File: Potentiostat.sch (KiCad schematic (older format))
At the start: 16 parts, among them U4 MAX6071BAUT21T, U5 LMP91000, U6 SPEC-110-902, U7 MCP6041T-I_OT

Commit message: layout wip
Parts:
- renumbered C10 to C11, C11 to C12, C12 to C13, C13 to C14, C14 to C15, C15 to C16, C16 to C17, R11 to R13, R12 to R14, R13 to R15, R14 to R16, R15 to R17, U4 to U5, U5 to U6, U6 to U7, U7 to U8
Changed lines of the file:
@@
 P 5800 4050
 AR Path="/605CEBF3" Ref="U?"  Part="1"
-AR Path="/605B4CA4/605CEBF3" Ref="U5"  Part="1"
-F 0 "U5" H 5350 5000 50  0000 C CNN
+AR Path="/605B4CA4/605CEBF3" Ref="U6"  Part="1"
+F 0 "U6" H 5350 5000 50  0000 C CNN
 F 1 "LMP91000" H 5850 5000 50  0000 C CNN
 F 2 "JetkovKiCADLib:LMP91000" H 5300 2900 50  0001 L BNN
@@
 P 5050 4700
 AR Path="/605CEBFB" Ref="#PWR?"  Part="1"
-AR Path="/605B4CA4/605CEBFB" Ref="#PWR045"  Part="1"
-F 0 "#PWR045" H 5050 4450 50  0001 C CNN
+AR Path="/605B4CA4/605CEBFB" Ref="#PWR048"  Part="1"
+F 0 "#PWR048" H 5050 4450 50  0001 C CNN
 F 1 "GND" H 5055 4527 50  0000 C CNN
 F 2 "" H 5050 4700 50  0001 C CNN
@@
 P 6650 3550
 AR Path="/605CEC09" Ref="R?"  Part="1"
-AR Path="/605B4CA4/605CEC09" Ref="R14"  Part="1"
-F 0 "R14" H 6720 3596 50  0000 L CNN
+AR Path="/605B4CA4/605CEC09" Ref="R16"  Part="1"
+F 0 "R16" H 6720 3596 50  0000 L CNN
 F 1 "49R9" H 6720 3505 50  0000 L CNN
 F 2 "JetkovKiCADLib:R_0402_NoSilk" V 6580 3550 50  0001 C CNN
@@
 P 7450 3850
 AR Path="/605CEC15" Ref="U?"  Part="1"
-AR Path="/605B4CA4/605CEC15" Ref="U6"  Part="1"
-F 0 "U6" H 7200 4200 50  0000 C CNN
+AR Path="/605B4CA4/605CEC15" Ref="U7"  Part="1"
+F 0 "U7" H 7200 4200 50  0000 C CNN
 F 1 "SPEC-110-902" H 7450 3500 50  0000 C CNN
 F 2 "JetkovKiCADLib:SPEC-110-902" H 7200 3250 50  0001 L BNN
@@
 P 6550 4300
 AR Path="/605CEC24" Ref="R?"  Part="1"
-AR Path="/605B4CA4/605CEC24" Ref="R13"  Part="1"
-F 0 "R13" H 6620 4346 50  0000 L CNN
+AR Path="/605B4CA4/605CEC24" Ref="R15"  Part="1"
+F 0 "R15" H 6620 4346 50  0000 L CNN
 F 1 "499k" H 6620 4255 50  0000 L CNN
 F 2 "JetkovKiCADLib:R_0402_NoSilk" V 6480 4300 50  0001 C CNN
@@
 P 6750 4300
 AR Path="/605CEC2A" Ref="C?"  Part="1"
-AR Path="/605B4CA4/605CEC2A" Ref="C15"  Part="1"
-F 0 "C15" H 6865 4346 50  0000 L CNN
+AR Path="/605B4CA4/605CEC2A" Ref="C16"  Part="1"
+F 0 "C16" H 6865 4346 50  0000 L CNN
 F 1 "DNP" H 6865 4255 50  0000 L CNB
 F 2 "JetkovKiCADLib:C_0402_NoSilk" H 6788 4150 50  0001 C CNN
@@
 P 4600 3450
 AR Path="/605CEC3F" Ref="C?"  Part="1"
-AR Path="/605B4CA4/605CEC3F" Ref="C14"  Part="1"
-F 0 "C14" H 4715 3496 50  0000 L CNN
+AR Path="/605B4CA4/605CEC3F" Ref="C15"  Part="1"
+F 0 "C15" H 4715 3496 50  0000 L CNN
 F 1 "1u" H 4715 3405 50  0000 L CNN
 F 2 "JetkovKiCADLib:C_0402_NoSilk" H 4638 3300 50  0001 C CNN
@@
 P 4600 3600
 AR Path="/605CEC45" Ref="#PWR?"  Part="1"
-AR Path="/605B4CA4/605CEC45" Ref="#PWR044"  Part="1"
-F 0 "#PWR044" H 4600 3350 50  0001 C CNN
+AR Path="/605B4CA4/605CEC45" Ref="#PWR047"  Part="1"
+F 0 "#PWR047" H 4600 3350 50  0001 C CNN
 F 1 "GND" H 4605 3427 50  0000 C CNN
 F 2 "" H 4600 3600 50  0001 C CNN
@@
 P 2350 3950
 AR Path="/605CEC51" Ref="U?"  Part="1"
-AR Path="/605B4CA4/605CEC51" Ref="U4"  Part="1"
-F 0 "U4" H 1900 4500 50  0000 C CNN
+AR Path="/605B4CA4/605CEC51" Ref="U5"  Part="1"
+F 0 "U5" H 1900 4500 50  0000 C CNN
 F 1 "MAX6071BAUT21T" H 2118 3695 50  0000 C CNN
 F 2 "JetkovKiCADLib:MAX6071BAUT21" H 1850 3150 50  0001 L BNN
@@
 P 2600 4100
 AR Path="/605CEC5C" Ref="#PWR?"  Part="1"
-AR Path="/605B4CA4/605CEC5C" Ref="#PWR039"  Part="1"
-F 0 "#PWR039" H 2600 3850 50  0001 C CNN
+AR Path="/605B4CA4/605CEC5C" Ref="#PWR042"  Part="1"
+F 0 "#PWR042" H 2600 3850 50  0001 C CNN
 F 1 "GND" H 2605 3927 50  0000 C CNN
 F 2 "" H 2600 4100 50  0001 C CNN
@@
 P 2900 3750
 AR Path="/605CEC62" Ref="C?"  Part="1"
-AR Path="/605B4CA4/605CEC62" Ref="C11"  Part="1"
-F 0 "C11" H 3015 3796 50  0000 L CNN
+AR Path="/605B4CA4/605CEC62" Ref="C12"  Part="1"
+F 0 "C12" H 3015 3796 50  0000 L CNN
 F 1 "0.1u" H 3015 3705 50  0000 L CNN
 F 2 "JetkovKiCADLib:C_0402_NoSilk" H 2938 3600 50  0001 C CNN
@@
 P 1000 3750
 AR Path="/605CEC69" Ref="C?"  Part="1"
-AR Path="/605B4CA4/605CEC69" Ref="C10"  Part="1"
-F 0 "C10" H 1115 3796 50  0000 L CNN
+AR Path="/605B4CA4/605CEC69" Ref="C11"  Part="1"
+F 0 "C11" H 1115 3796 50  0000 L CNN
 F 1 "0.1u" H 1115 3705 50  0000 L CNN
 F 2 "JetkovKiCADLib:C_0402_NoSilk" H 1038 3600 50  0001 C CNN
@@
 P 1000 3900
 AR Path="/605CEC6F" Ref="#PWR?"  Part="1"
-AR Path="/605B4CA4/605CEC6F" Ref="#PWR037"  Part="1"
-F 0 "#PWR037" H 1000 3650 50  0001 C CNN
+AR Path="/605B4CA4/605CEC6F" Ref="#PWR040"  Part="1"
+F 0 "#PWR040" H 1000 3650 50  0001 C CNN
 F 1 "GND" H 1005 3727 50  0000 C CNN
 F 2 "" H 1000 3900 50  0001 C CNN
@@
 P 1650 4400
 AR Path="/605CEC76" Ref="#PWR?"  Part="1"
-AR Path="/605B4CA4/605CEC76" Ref="#PWR038"  Part="1"
-F 0 "#PWR038" H 1650 4150 50  0001 C CNN
+AR Path="/605B4CA4/605CEC76" Ref="#PWR041"  Part="1"
+F 0 "#PWR041" H 1650 4150 50  0001 C CNN
 F 1 "GND" H 1655 4227 50  0000 C CNN
 F 2 "" H 1650 4400 50  0001 C CNN
@@
 P 1650 4250
 AR Path="/605CEC7C" Ref="R?"  Part="1"
-AR Path="/605B4CA4/605CEC7C" Ref="R11"  Part="1"
-F 0 "R11" H 1720 4296 50  0000 L CNN
+AR Path="/605B4CA4/605CEC7C" Ref="R13"  Part="1"
+F 0 "R13" H 1720 4296 50  0000 L CNN
 F 1 "1M" H 1720 4205 50  0000 L CNN
 F 2 "JetkovKiCADLib:R_0402_NoSilk" V 1580 4250 50  0001 C CNN
@@
 P 1000 3500
 AR Path="/605CEC87" Ref="#PWR?"  Part="1"
-AR Path="/605B4CA4/605CEC87" Ref="#PWR036"  Part="1"
-F 0 "#PWR036" H 1000 3350 50  0001 C CNN
+AR Path="/605B4CA4/605CEC87" Ref="#PWR039"  Part="1"
+F 0 "#PWR039" H 1000 3350 50  0001 C CNN
 F 1 "VDD" H 1015 3673 50  0000 C CNN
 F 2 "" H 1000 3500 50  0001 C CNN
@@
 P 3200 3750
 AR Path="/605CEC91" Ref="R?"  Part="1"
-AR Path="/605B4CA4/605CEC91" Ref="R12"  Part="1"
-F 0 "R12" H 3270 3796 50  0000 L CNN
+AR Path="/605B4CA4/605CEC91" Ref="R14"  Part="1"
+F 0 "R14" H 3270 3796 50  0000 L CNN
 F 1 "DNP" H 3270 3705 50  0000 L CNB
 F 2 "JetkovKiCADLib:R_0402_NoSilk" V 3130 3750 50  0001 C CNN
@@
 P 3200 4050
 AR Path="/605CEC97" Ref="C?"  Part="1"
-AR Path="/605B4CA4/605CEC97" Ref="C12"  Part="1"
-F 0 "C12" H 3315 4096 50  0000 L CNN
+AR Path="/605B4CA4/605CEC97" Ref="C13"  Part="1"
+F 0 "C13" H 3315 4096 50  0000 L CNN
 F 1 "DNP" H 3315 4005 50  0000 L CNB
 F 2 "JetkovKiCADLib:C_0402_NoSilk" H 3238 3900 50  0001 C CNN
@@
 P 3200 4200
 AR Path="/605CEC9D" Ref="#PWR?"  Part="1"
-AR Path="/605B4CA4/605CEC9D" Ref="#PWR041"  Part="1"
-F 0 "#PWR041" H 3200 3950 50  0001 C CNN
+AR Path="/605B4CA4/605CEC9D" Ref="#PWR044"  Part="1"
+F 0 "#PWR044" H 3200 3950 50  0001 C CNN
 F 1 "GND" H 3205 4027 50  0000 C CNN
 F 2 "" H 3200 4200 50  0001 C CNN
@@
 P 2900 3900
 AR Path="/605CECA5" Ref="#PWR?"  Part="1"
-AR Path="/605B4CA4/605CECA5" Ref="#PWR040"  Part="1"
-F 0 "#PWR040" H 2900 3650 50  0001 C CNN
+AR Path="/605B4CA4/605CECA5" Ref="#PWR043"  Part="1"
+F 0 "#PWR043" H 2900 3650 50  0001 C CNN
 F 1 "GND" H 2905 3727 50  0000 C CNN
 F 2 "" H 2900 3900 50  0001 C CNN
@@
 P 4400 3450
 AR Path="/605CECB0" Ref="C?"  Part="1"
-AR Path="/605B4CA4/605CECB0" Ref="C13"  Part="1"
-F 0 "C13" H 4515 3496 50  0000 L CNN
+AR Path="/605B4CA4/605CECB0" Ref="C14"  Part="1"
+F 0 "C14" H 4515 3496 50  0000 L CNN
 F 1 "0.1u" H 4515 3405 50  0000 L CNN
 F 2 "JetkovKiCADLib:C_0402_NoSilk" H 4438 3300 50  0001 C CNN
@@
 P 4400 3600
 AR Path="/605CECB6" Ref="#PWR?"  Part="1"
-AR Path="/605B4CA4/605CECB6" Ref="#PWR043"  Part="1"
-F 0 "#PWR043" H 4400 3350 50  0001 C CNN
+AR Path="/605B4CA4/605CECB6" Ref="#PWR046"  Part="1"
+F 0 "#PWR046" H 4400 3350 50  0001 C CNN
 F 1 "GND" H 4405 3427 50  0000 C CNN
 F 2 "" H 4400 3600 50  0001 C CNN
@@
 P 4400 3200
 AR Path="/605CECC4" Ref="#PWR?"  Part="1"
-AR Path="/605B4CA4/605CECC4" Ref="#PWR042"  Part="1"
-F 0 "#PWR042" H 4400 3050 50  0001 C CNN
+AR Path="/605B4CA4/605CECC4" Ref="#PWR045"  Part="1"
+F 0 "#PWR045" H 4400 3050 50  0001 C CNN
 F 1 "VDD" H 4415 3373 50  0000 C CNN
 F 2 "" H 4400 3200 50  0001 C CNN
@@
 P 9600 3950
 AR Path="/605CECCE" Ref="U?"  Part="1"
-AR Path="/605B4CA4/605CECCE" Ref="U7"  Part="1"
-F 0 "U7" H 9650 4250 50  0000 L CNN
+AR Path="/605B4CA4/605CECCE" Ref="U8"  Part="1"
+F 0 "U8" H 9650 4250 50  0000 L CNN
 F 1 "MCP6041T-I_OT" H 9650 4150 50  0000 L CNN
 F 2 "JetkovKiCADLib:MCP6041T-I_OT" H 9900 3550 50  0001 L BNN
@@
 P 9550 3450
 AR Path="/605CECD4" Ref="#PWR?"  Part="1"
-AR Path="/605B4CA4/605CECD4" Ref="#PWR046"  Part="1"
-F 0 "#PWR046" H 9550 3300 50  0001 C CNN
+AR Path="/605B4CA4/605CECD4" Ref="#PWR049"  Part="1"
+F 0 "#PWR049" H 9550 3300 50  0001 C CNN
 F 1 "VDD" H 9565 3623 50  0000 C CNN
 F 2 "" H 9550 3450 50  0001 C CNN
@@
 P 9550 4300
 AR Path="/605CECDA" Ref="#PWR?"  Part="1"
-AR Path="/605B4CA4/605CECDA" Ref="#PWR047"  Part="1"
-F 0 "#PWR047" H 9550 4050 50  0001 C CNN
+AR Path="/605B4CA4/605CECDA" Ref="#PWR050"  Part="1"
+F 0 "#PWR050" H 9550 4050 50  0001 C CNN
 F 1 "GND" H 9555 4127 50  0000 C CNN
 F 2 "" H 9550 4300 50  0001 C CNN
@@
 P 10050 3500
 AR Path="/605CECE8" Ref="C?"  Part="1"
-AR Path="/605B4CA4/605CECE8" Ref="C16"  Part="1"
-F 0 "C16" V 9800 3450 50  0000 L CNN
+AR Path="/605B4CA4/605CECE8" Ref="C17"  Part="1"
+F 0 "C17" V 9800 3450 50  0000 L CNN
 F 1 "0.1u" V 9900 3400 50  0000 L CNN
 F 2 "JetkovKiCADLib:C_0402_NoSilk" H 10088 3350 50  0001 C CNN
@@
 P 10450 3550
 AR Path="/605CECEE" Ref="#PWR?"  Part="1"
-AR Path="/605B4CA4/605CECEE" Ref="#PWR048"  Part="1"
-F 0 "#PWR048" H 10450 3300 50  0001 C CNN
+AR Path="/605B4CA4/605CECEE" Ref="#PWR051"  Part="1"
+F 0 "#PWR051" H 10450 3300 50  0001 C CNN
 F 1 "GND" H 10455 3377 50  0000 C CNN
 F 2 "" H 10450 3550 50  0001 C CNN
@@
 P 9050 4150
 AR Path="/605CECFA" Ref="R?"  Part="1"
-AR Path="/605B4CA4/605CECFA" Ref="R15"  Part="1"
-F 0 "R15" H 9120 4196 50  0000 L CNN
+AR Path="/605B4CA4/605CECFA" Ref="R17"  Part="1"
+F 0 "R17" H 9120 4196 50  0000 L CNN
 F 1 "DNP" H 9120 4105 50  0000 L CNB
 F 2 "JetkovKiCADLib:R_0402_NoSilk" V 8980 4150 50  0001 C CNN

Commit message: Add resistor details
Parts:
- R15: Description (none) -> RES 499K OHM 1% 1/16W 0402; Manufacturer (none) -> Stackpole Electronics Inc; Part Number (none) -> RMCF0402FT499K; Temp Range (none) -> -55°C +155°C
- R16: Description (none) -> RES 49.9 OHM 1% 1/16W 0402; Manufacturer (none) -> Stackpole Electronics Inc; Part Number (none) -> RMCF0402FT49R9; Temp Range (none) -> -55°C +155°C
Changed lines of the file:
@@
 F 1 "49R9" H 6720 3505 50  0000 L CNN
 F 2 "JetkovKiCADLib:R_0402_NoSilk" V 6580 3550 50  0001 C CNN
-F 3 "~" H 6650 3550 50  0001 C CNN
+F 3 "https://www.seielect.com/catalog/sei-rmcf_rmcp.pdf" H 6650 3550 50  0001 C CNN
+F 4 "RES 49.9 OHM 1% 1/16W 0402" H 6650 3550 50  0001 C CNN "Description"
+F 5 "Stackpole Electronics Inc" H 6650 3550 50  0001 C CNN "Manufacturer"
+F 6 "RMCF0402FT49R9" H 6650 3550 50  0001 C CNN "Part Number"
+F 7 "-55°C +155°C" H 6650 3550 50  0001 C CNN "Temp Range"
 	1    6650 3550
 	-1   0    0    -1
@@
 F 1 "499k" H 6620 4255 50  0000 L CNN
 F 2 "JetkovKiCADLib:R_0402_NoSilk" V 6480 4300 50  0001 C CNN
-F 3 "~" H 6550 4300 50  0001 C CNN
+F 3 "https://www.seielect.com/catalog/sei-rmcf_rmcp.pdf" H 6550 4300 50  0001 C CNN
+F 4 "RES 499K OHM 1% 1/16W 0402" H 6550 4300 50  0001 C CNN "Description"
+F 5 "Stackpole Electronics Inc" H 6550 4300 50  0001 C CNN "Manufacturer"
+F 6 "RMCF0402FT499K" H 6550 4300 50  0001 C CNN "Part Number"
+F 7 "-55°C +155°C" H 6550 4300 50  0001 C CNN "Temp Range"
 	1    6550 4300
 	-1   0    0    -1
@@
 F 2 "JetkovKiCADLib:C_0402_NoSilk" H 6788 4150 50  0001 C CNN
 F 3 "~" H 6750 4300 50  0001 C CNN
+F 4 "~" H 6750 4300 50  0001 C CNN "Description"
+F 5 "~" H 6750 4300 50  0001 C CNN "Manufacturer"
+F 6 "~" H 6750 4300 50  0001 C CNN "Part Number"
+F 7 "~" H 6750 4300 50  0001 C CNN "Temp Range"
 	1    6750 4300
 	1    0    0    -1
@@
 F 2 "JetkovKiCADLib:R_0402_NoSilk" V 3130 3750 50  0001 C CNN
 F 3 "~" H 3200 3750 50  0001 C CNN
+F 4 "~" H 3200 3750 50  0001 C CNN "Description"
+F 5 "~" H 3200 3750 50  0001 C CNN "Manufacturer"
+F 6 "~" H 3200 3750 50  0001 C CNN "Part Number"
+F 7 "~" H 3200 3750 50  0001 C CNN "Temp Range"
 	1    3200 3750
 	1    0    0    -1
@@
 F 2 "JetkovKiCADLib:C_0402_NoSilk" H 3238 3900 50  0001 C CNN
 F 3 "~" H 3200 4050 50  0001 C CNN
+F 4 "~" H 3200 4050 50  0001 C CNN "Description"
+F 5 "~" H 3200 4050 50  0001 C CNN "Manufacturer"
+F 6 "~" H 3200 4050 50  0001 C CNN "Part Number"
+F 7 "~" H 3200 4050 50  0001 C CNN "Temp Range"
 	1    3200 4050
 	1    0    0    -1
@@
 F 2 "JetkovKiCADLib:R_0402_NoSilk" V 8980 4150 50  0001 C CNN
 F 3 "~" H 9050 4150 50  0001 C CNN
+F 4 "~" H 9050 4150 50  0001 C CNN "Description"
+F 5 "~" H 9050 4150 50  0001 C CNN "Manufacturer"
+F 6 "~" H 9050 4150 50  0001 C CNN "Part Number"
+F 7 "~" H 9050 4150 50  0001 C CNN "Temp Range"
 	1    9050 4150
 	-1   0    0    -1

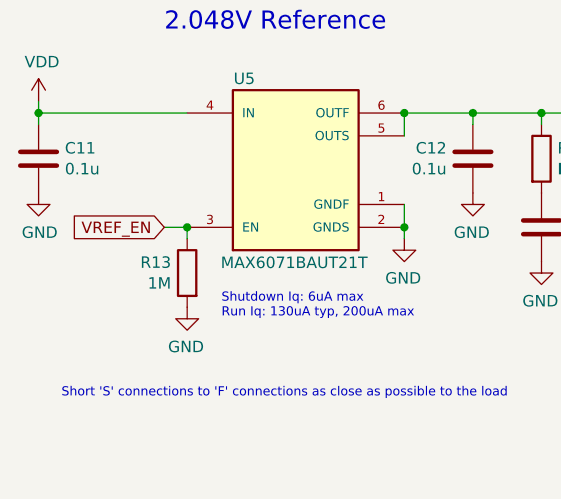
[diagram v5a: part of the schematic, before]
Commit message: Fill in component info, reduce uniqe resistors. cleanup
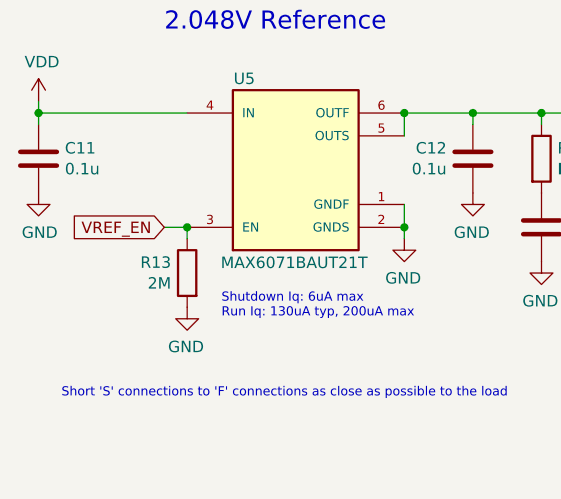
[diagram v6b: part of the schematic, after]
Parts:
- R13: value 1M -> 2M; Description (none) -> RES 2M OHM 1% 1/16W 0402; Manufacturer (none) -> Stackpole Electronics Inc; Part Number (none) -> RMCF0402FT2M00; Temp Range (none) -> -55°C +155°C
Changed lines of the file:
@@
 AR Path="/605B4CA4/605CEC7C" Ref="R13"  Part="1"
 F 0 "R13" H 1720 4296 50  0000 L CNN
-F 1 "1M" H 1720 4205 50  0000 L CNN
+F 1 "2M" H 1720 4205 50  0000 L CNN
 F 2 "JetkovKiCADLib:R_0402_NoSilk" V 1580 4250 50  0001 C CNN
-F 3 "~" H 1650 4250 50  0001 C CNN
+F 3 "https://www.seielect.com/catalog/sei-rmcf_rmcp.pdf" H 1650 4250 50  0001 C CNN
+F 4 "RES 2M OHM 1% 1/16W 0402" H 1650 4250 50  0001 C CNN "Description"
+F 5 "Stackpole Electronics Inc" H 1650 4250 50  0001 C CNN "Manufacturer"
+F 6 "RMCF0402FT2M00" H 1650 4250 50  0001 C CNN "Part Number"
+F 7 "-55°C +155°C" H 1650 4250 50  0001 C CNN "Temp Range"
 	1    1650 4250
 	-1   0    0    -1

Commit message: Info tweaks
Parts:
- U7: value SPEC-110-902 -> DNP
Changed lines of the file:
@@
 AR Path="/605B4CA4/605CEC15" Ref="U7"  Part="1"
 F 0 "U7" H 7200 4200 50  0000 C CNN
-F 1 "SPEC-110-902" H 7450 3500 50  0000 C CNN
+F 1 "DNP" H 7450 3500 50  0000 C CNN
 F 2 "JetkovKiCADLib:SPEC-110-902" H 7200 3250 50  0001 L BNN
 F 3 "http://www.spec-sensors.com/wp-content/uploads/2016/06/RESP_IRR_20-C-Package-110-902.pdf" H 7750 3400 50  0001 L BNN

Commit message: Tweak component infos
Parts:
- U7: value DNP -> 110-902
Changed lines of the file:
@@
 AR Path="/605B4CA4/605CEC15" Ref="U7"  Part="1"
 F 0 "U7" H 7200 4200 50  0000 C CNN
-F 1 "DNP" H 7450 3500 50  0000 C CNN
+F 1 "110-902" H 7450 3500 50  0000 C CNN
 F 2 "JetkovKiCADLib:SPEC-110-902" H 7200 3250 50  0001 L BNN
 F 3 "http://www.spec-sensors.com/wp-content/uploads/2016/06/RESP_IRR_20-C-Package-110-902.pdf" H 7750 3400 50  0001 L BNN
